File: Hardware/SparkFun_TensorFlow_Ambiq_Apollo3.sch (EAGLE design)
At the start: 102 parts, among them J5 CORTEX_DEBUG_PTH, J6 CAMERA-OV7670, M1 MEMS_MIC, M2 MEMS_MIC, U1 AMBIQ-APOLLO3KBR, U2 LIS2DH12, U3 1.8V, U4 LMV358, Y1 32MHz, Y2 32.768kHz

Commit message: Updating components to SparkFun ibraries
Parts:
- C1: device ambiq:0.47UF-0402-TIGHT-6.3V-10% -> SparkFun-Capacitors:470NF-0402_TIGHT-6.3V-10%-X5R
- C11: device ambiq:47NF-0402-TIGHT-25V-10% -> SparkFun-Capacitors:47NF-0402_TIGHT-25V-10%-X7R
- C16, C3, C5, C8: device ambiq:2.2UF-0402-TIGHT-25V-10% -> SparkFun-Capacitors:2.2UF-0402_TIGHT-10V-10%-X5R
- C18: device ambiq:0.5PF-0402-0.5PF-1% -> SparkFun-Capacitors:0.5PF-0402_TIGHT-20V-PM0.05PF-NP0
- C2: device ambiq:4.7UF-0402-TIGHT-6.3V-(20%) -> SparkFun-Capacitors:4.7UF-0402_TIGHT-6.3V-20%-X5R
- C28: device ambiq:1.0NF/1000PF-0402-50V-10% -> SparkFun-Capacitors:1.0NF/1000PF-0402_TIGHT-50V-10%
- J6: device ambiq:CAMERA-OV7670 -> SparkFun-Connectors:CAMERA-OV7670
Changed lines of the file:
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@@
 <part name="L2" library="ambiq" deviceset="INDUCTOR" device="-0805-1.0UH" value="1.0uH"/>
 <part name="GND3" library="SparkFun-PowerSymbols" deviceset="GND" device=""/>
-<part name="C2" library="ambiq" deviceset="4.7UF" device="-0402-TIGHT-6.3V-(20%)" value="4.7uF"/>
+<part name="C2" library="SparkFun-Capacitors" deviceset="4.7UF" device="-0402_TIGHT-6.3V-20%-X5R" value="4.7uF"/>
 <part name="C4" library="ambiq" deviceset="1.0UF" device="-0402-TIGHT-16V-10%" value="1.0uF"/>
 <part name="GND6" library="SparkFun-PowerSymbols" deviceset="GND" device=""/>
@@
 <part name="GND16" library="SparkFun-PowerSymbols" deviceset="GND" device=""/>
 <part name="R3" library="ambiq" deviceset="10KOHM" device="-0402-TIGHT-1/10W-1%" value="10k"/>
-<part name="C1" library="ambiq" deviceset="0.47UF" device="-0402-TIGHT-6.3V-10%" value="0.47uF"/>
-<part name="C3" library="ambiq" deviceset="2.2UF" device="-0402-TIGHT-25V-10%" value="2.2uF"/>
-<part name="C5" library="ambiq" deviceset="2.2UF" device="-0402-TIGHT-25V-10%" value="2.2uF"/>
-<part name="C8" library="ambiq" deviceset="2.2UF" device="-0402-TIGHT-25V-10%" value="2.2uF"/>
+<part name="C1" library="SparkFun-Capacitors" deviceset="470NF" device="-0402_TIGHT-6.3V-10%-X5R" value="0.47uF"/>
+<part name="C3" library="SparkFun-Capacitors" deviceset="2.2UF" device="-0402_TIGHT-10V-10%-X5R" value="2.2uF"/>
+<part name="C5" library="SparkFun-Capacitors" deviceset="2.2UF" device="-0402_TIGHT-10V-10%-X5R" value="2.2uF"/>
+<part name="C8" library="SparkFun-Capacitors" deviceset="2.2UF" device="-0402_TIGHT-10V-10%-X5R" value="2.2uF"/>
 <part name="GND8" library="SparkFun-PowerSymbols" deviceset="GND" device=""/>
 <part name="GND7" library="SparkFun-PowerSymbols" deviceset="GND" device=""/>
@@
 <part name="C14" library="ambiq" deviceset="1.0UF" device="-0402-TIGHT-16V-10%" value="1.0uF"/>
 <part name="C15" library="ambiq" deviceset="1.0UF" device="-0402-TIGHT-16V-10%" value="1.0uF"/>
-<part name="C11" library="ambiq" deviceset="47NF" device="-0402-TIGHT-25V-10%" value="47nF"/>
-<part name="C16" library="ambiq" deviceset="2.2UF" device="-0402-TIGHT-25V-10%" value="2.2uF"/>
+<part name="C11" library="SparkFun-Capacitors" deviceset="47NF" device="-0402_TIGHT-25V-10%-X7R" value="47nF"/>
+<part name="C16" library="SparkFun-Capacitors" deviceset="2.2UF" device="-0402_TIGHT-10V-10%-X5R" value="2.2uF"/>
 <part name="GND10" library="SparkFun-PowerSymbols" deviceset="GND" device=""/>
 <part name="GND11" library="SparkFun-PowerSymbols" deviceset="GND" device=""/>
@@
 <part name="C17" library="ambiq" deviceset="DNP-CAP" device="-0402-TIGHT" value="DNP"/>
 <part name="L3" library="ambiq" deviceset="INDUCTOR" device="-0402-2.7NH" value="2.7nH"/>
-<part name="C18" library="ambiq" deviceset="0.5PF" device="-0402-0.5PF-1%" value="0.5pF"/>
+<part name="C18" library="SparkFun-Capacitors" deviceset="0.5PF" device="-0402_TIGHT-20V-PM0.05PF-NP0" value="0.5pF"/>
 <part name="L4" library="ambiq" deviceset="INDUCTOR" device="-0402-2.0NH" value="2.0nH"/>
 <part name="GND21" library="SparkFun-PowerSymbols" deviceset="GND" device=""/>
@@
 <part name="M1" library="ambiq" deviceset="MEMS_MICROPHONE" device="SPW2430HR5H-B" value="MEMS_MIC"/>
 <part name="M2" library="ambiq" deviceset="MEMS_MICROPHONE" device="SPW2430HR5H-B" value="MEMS_MIC"/>
-<part name="J6" library="ambiq" deviceset="CAMERA-OV7670" device=""/>
+<part name="J6" library="SparkFun-Connectors" deviceset="CAMERA-OV7670" device=""/>
 <part name="BT1" library="SparkFun-Batteries" deviceset="BATTERY" device="-20MM_SMD_4LEGS_OVERPASTE_INNER"/>
 <part name="H4" library="SparkFun-Hardware" deviceset="STAND-OFF" device=""/>
@@
 <part name="TP1" library="SparkFun-Connectors" deviceset="TEST-POINT" device="3X5"/>
 <part name="TP2" library="SparkFun-Connectors" deviceset="TEST-POINT" device="3X5"/>
-<part name="C28" library="ambiq" deviceset="1.0NF/1000PF" device="-0402-50V-10%" value="1.0nF"/>
+<part name="C28" library="SparkFun-Capacitors" deviceset="1.0NF/1000PF" device="-0402_TIGHT-50V-10%" value="1.0nF"/>
 <part name="GND42" library="SparkFun-PowerSymbols" deviceset="GND" device=""/>
 <part name="TP3" library="SparkFun-Connectors" deviceset="TEST-POINT" device="3X5"/>

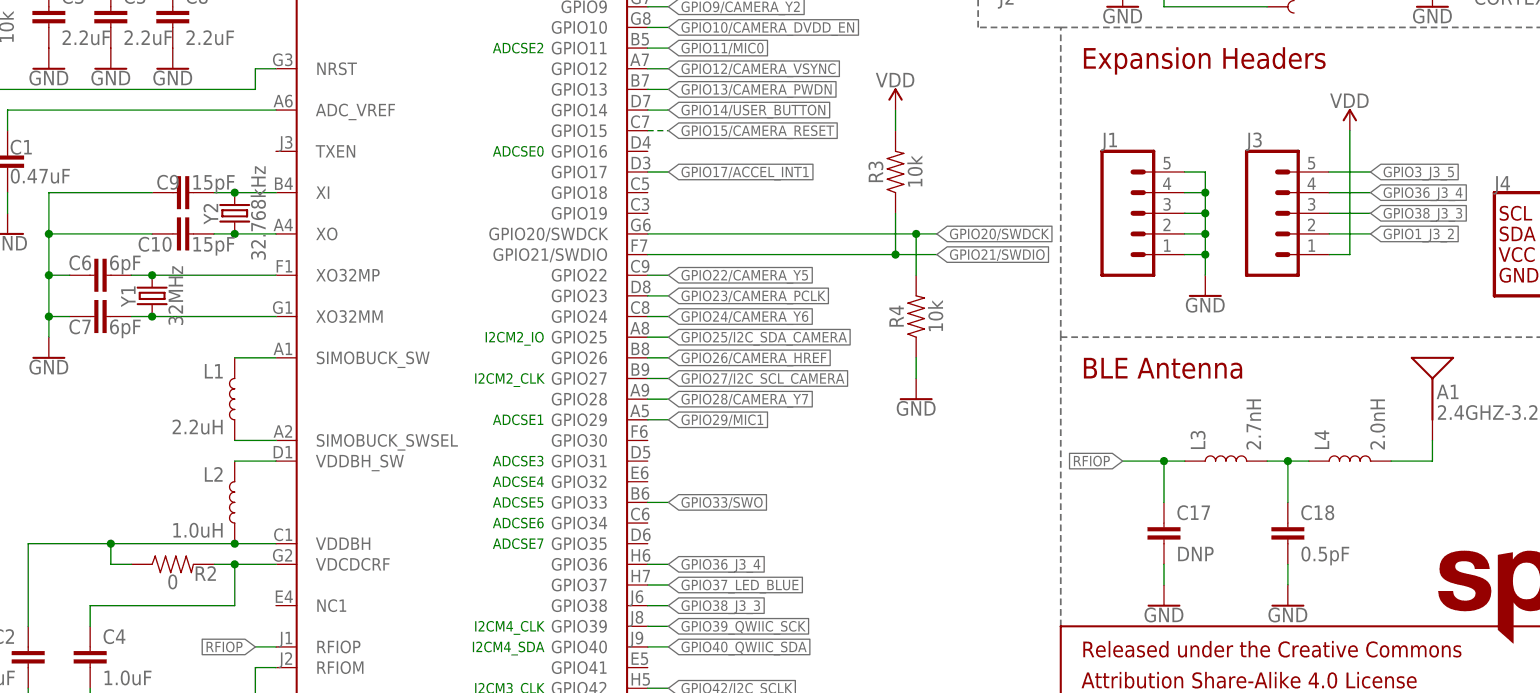
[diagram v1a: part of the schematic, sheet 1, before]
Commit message: Continue adding parts from SparkFun library
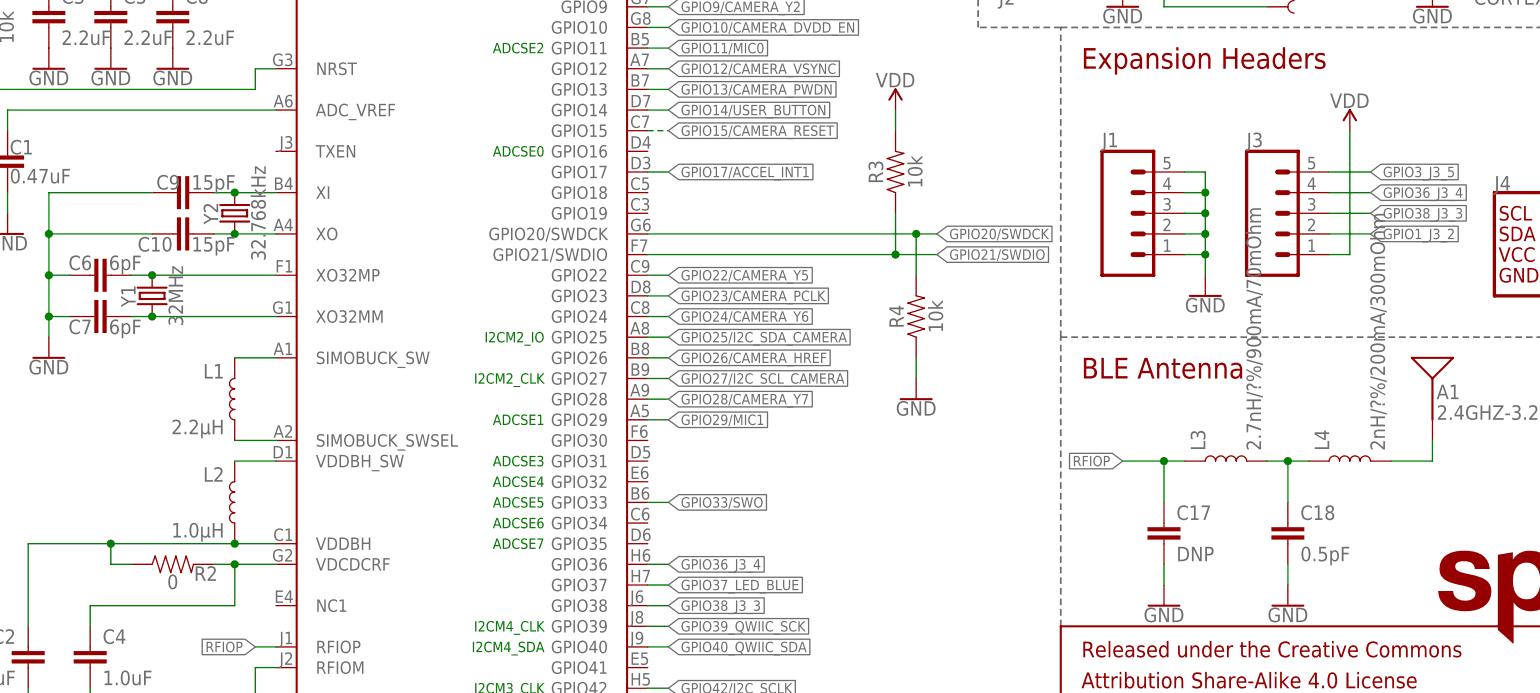
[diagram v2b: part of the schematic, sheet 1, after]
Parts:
- L1: value 2.2uH -> 2.2μH; device ambiq:INDUCTOR-0805-2.2UH -> SparkFun-Coils:2.2μH-0805_WIDE-2.2μH-1.7A-0.14OHM
- L2: value 1.0uH -> 1.0μH; device ambiq:INDUCTOR-0805-1.0UH -> SparkFun-Coils:1.0μH-0805_WIDE-1.0μH-1.4A-0.07OHM
- L3: value 2.7nH -> 2.7nH/?%/900mA/70mOhm; device ambiq:INDUCTOR-0402-2.7NH -> SparkFun-Coils:INDUCTOR-0402_TIGHT-2.7NH
- L4: value 2.0nH -> 2nH/?%/200mA/300mOhm; device ambiq:INDUCTOR-0402-2.0NH -> SparkFun-Coils:INDUCTOR-0402_TIGHT-2.0NH
- M1, M2: device ambiq:MEMS_MICROPHONESPW2430HR5H-B -> SparkFun-Sensors:MEMS_MICROPHONESPW2430HR5H-B
- R18: device ambiq:22KOHM-0402-1/16W-1% -> SparkFun-Resistors:22KOHM-0402_TIGHT-1/10W-1%
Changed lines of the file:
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@@
 <part name="R1" library="ambiq" deviceset="10KOHM" device="-0402-TIGHT-1/10W-1%" value="10k"/>
 <part name="GND5" library="SparkFun-PowerSymbols" deviceset="GND" device=""/>
-<part name="L1" library="ambiq" deviceset="INDUCTOR" device="-0805-2.2UH" value="2.2uH"/>
-<part name="L2" library="ambiq" deviceset="INDUCTOR" device="-0805-1.0UH" value="1.0uH"/>
+<part name="L1" library="SparkFun-Coils" deviceset="2.2μH" device="-0805_WIDE-2.2μH-1.7A-0.14OHM" value="2.2μH"/>
+<part name="L2" library="SparkFun-Coils" deviceset="1.0μH" device="-0805_WIDE-1.0μH-1.4A-0.07OHM" value="1.0μH"/>
 <part name="GND3" library="SparkFun-PowerSymbols" deviceset="GND" device=""/>
 <part name="C2" library="SparkFun-Capacitors" deviceset="4.7UF" device="-0402_TIGHT-6.3V-20%-X5R" value="4.7uF"/>
@@
 <part name="GND15" library="SparkFun-PowerSymbols" deviceset="GND" device=""/>
 <part name="C17" library="ambiq" deviceset="DNP-CAP" device="-0402-TIGHT" value="DNP"/>
-<part name="L3" library="ambiq" deviceset="INDUCTOR" device="-0402-2.7NH" value="2.7nH"/>
+<part name="L3" library="SparkFun-Coils" deviceset="INDUCTOR" device="-0402_TIGHT-2.7NH" value="2.7nH/?%/900mA/70mOhm"/>
 <part name="C18" library="SparkFun-Capacitors" deviceset="0.5PF" device="-0402_TIGHT-20V-PM0.05PF-NP0" value="0.5pF"/>
-<part name="L4" library="ambiq" deviceset="INDUCTOR" device="-0402-2.0NH" value="2.0nH"/>
+<part name="L4" library="SparkFun-Coils" deviceset="INDUCTOR" device="-0402_TIGHT-2.0NH" value="2nH/?%/200mA/300mOhm"/>
 <part name="GND21" library="SparkFun-PowerSymbols" deviceset="GND" device=""/>
 <part name="GND17" library="SparkFun-PowerSymbols" deviceset="GND" device=""/>
@@
 <part name="GND24" library="SparkFun-PowerSymbols" deviceset="GND" device=""/>
 <part name="R2" library="ambiq" deviceset="0OHM" device="-0402-TIGHT-1/10W-5%" value="0"/>
-<part name="M1" library="ambiq" deviceset="MEMS_MICROPHONE" device="SPW2430HR5H-B" value="MEMS_MIC"/>
-<part name="M2" library="ambiq" deviceset="MEMS_MICROPHONE" device="SPW2430HR5H-B" value="MEMS_MIC"/>
+<part name="M1" library="SparkFun-Sensors" deviceset="MEMS_MICROPHONE" device="SPW2430HR5H-B" value="MEMS_MIC"/>
+<part name="M2" library="SparkFun-Sensors" deviceset="MEMS_MICROPHONE" device="SPW2430HR5H-B" value="MEMS_MIC"/>
 <part name="J6" library="SparkFun-Connectors" deviceset="CAMERA-OV7670" device=""/>
 <part name="BT1" library="SparkFun-Batteries" deviceset="BATTERY" device="-20MM_SMD_4LEGS_OVERPASTE_INNER"/>
@@
 <part name="GND25" library="SparkFun-PowerSymbols" deviceset="GND" device=""/>
 <part name="R19" library="ambiq" deviceset="10KOHM" device="-0402-TIGHT-1/10W-1%" value="10k"/>
-<part name="R18" library="ambiq" deviceset="22KOHM" device="-0402-1/16W-1%" value="22k"/>
+<part name="R18" library="SparkFun-Resistors" deviceset="22KOHM" device="-0402_TIGHT-1/10W-1%" value="22k"/>
 <part name="SUPPLY31" library="SparkFun-PowerSymbols" deviceset="VDD" device=""/>
 <part name="GND37" library="SparkFun-PowerSymbols" deviceset="GND" device=""/>

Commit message: Finish converting parts to SparkFun library
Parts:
- R1, R10, R11, R19, R22, R25, R26, R3, R4, R9: device ambiq:10KOHM-0402-TIGHT-1/10W-1% -> SparkFun-Resistors:10KOHM-0402_TIGHT-1/10W-1%
- R2: device ambiq:0OHM-0402-TIGHT-1/10W-5% -> SparkFun-Resistors:0OHM-0402_TIGHT-1/16W
- U1: device ambiq:AMBIQ-APOLLO3KBR -> SparkFun-IC-Microcontroller:AMBIQ-APOLLO3KBR
- U2: device ambiq:LIS2DH12 -> SparkFun-Sensors:LIS2DH12
- U3: device ambiq:V_REG_AP2127K-2.8 -> SparkFun-IC-Power:V_REG_AP2127K-1.8V
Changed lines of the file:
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@@
 </classes>
 <parts>
-<part name="U1" library="ambiq" deviceset="AMBIQ-APOLLO3" device="KBR"/>
+<part name="U1" library="SparkFun-IC-Microcontroller" deviceset="AMBIQ-APOLLO3" device="KBR"/>
 <part name="FRAME1" library="SparkFun-Aesthetics" deviceset="FRAME-LETTER" device=""/>
 <part name="J2" library="SparkFun-Connectors" deviceset="6_PIN_SERIAL_TARGET" device="SMD"/>
@@
 <part name="C9" library="ambiq" deviceset="15PF" device="-0402-TIGHT-50V-5%" value="15pF"/>
 <part name="C10" library="ambiq" deviceset="15PF" device="-0402-TIGHT-50V-5%" value="15pF"/>
-<part name="R1" library="ambiq" deviceset="10KOHM" device="-0402-TIGHT-1/10W-1%" value="10k"/>
+<part name="R1" library="SparkFun-Resistors" deviceset="10KOHM" device="-0402_TIGHT-1/10W-1%" value="10k"/>
 <part name="GND5" library="SparkFun-PowerSymbols" deviceset="GND" device=""/>
 <part name="L1" library="SparkFun-Coils" deviceset="2.2μH" device="-0805_WIDE-2.2μH-1.7A-0.14OHM" value="2.2μH"/>
@@
 <part name="GND9" library="SparkFun-PowerSymbols" deviceset="GND" device=""/>
 <part name="GND2" library="SparkFun-PowerSymbols" deviceset="GND" device=""/>
-<part name="R4" library="ambiq" deviceset="10KOHM" device="-0402-TIGHT-1/10W-1%" value="10k"/>
+<part name="R4" library="SparkFun-Resistors" deviceset="10KOHM" device="-0402_TIGHT-1/10W-1%" value="10k"/>
 <part name="GND16" library="SparkFun-PowerSymbols" deviceset="GND" device=""/>
-<part name="R3" library="ambiq" deviceset="10KOHM" device="-0402-TIGHT-1/10W-1%" value="10k"/>
+<part name="R3" library="SparkFun-Resistors" deviceset="10KOHM" device="-0402_TIGHT-1/10W-1%" value="10k"/>
 <part name="C1" library="SparkFun-Capacitors" deviceset="470NF" device="-0402_TIGHT-6.3V-10%-X5R" value="0.47uF"/>
 <part name="C3" library="SparkFun-Capacitors" deviceset="2.2UF" device="-0402_TIGHT-10V-10%-X5R" value="2.2uF"/>
@@
 <part name="J5" library="SparkFun-Connectors" deviceset="CORTEX_DEBUG" device="_PTH" value="CORTEX_DEBUG_PTH"/>
 <part name="GND24" library="SparkFun-PowerSymbols" deviceset="GND" device=""/>
-<part name="R2" library="ambiq" deviceset="0OHM" device="-0402-TIGHT-1/10W-5%" value="0"/>
+<part name="R2" library="SparkFun-Resistors" deviceset="0OHM" device="-0402_TIGHT-1/16W" value="0"/>
 <part name="M1" library="SparkFun-Sensors" deviceset="MEMS_MICROPHONE" device="SPW2430HR5H-B" value="MEMS_MIC"/>
 <part name="M2" library="SparkFun-Sensors" deviceset="MEMS_MICROPHONE" device="SPW2430HR5H-B" value="MEMS_MIC"/>
@@
 <part name="SUPPLY1" library="SparkFun-PowerSymbols" deviceset="V_BATT" device=""/>
 <part name="GND1" library="SparkFun-PowerSymbols" deviceset="GND" device=""/>
-<part name="U2" library="ambiq" deviceset="LIS2DH12" device=""/>
+<part name="U2" library="SparkFun-Sensors" deviceset="LIS2DH12" device=""/>
 <part name="C21" library="SparkFun-Capacitors" deviceset="10UF" device="-0603-6.3V-20%" value="10uF"/>
 <part name="C20" library="ambiq" deviceset="0.1UF" device="-0402-TIGHT-16V-10%" value="0.1uF"/>
@@
 <part name="SUPPLY22" library="SparkFun-PowerSymbols" deviceset="VDD" device=""/>
 <part name="GND32" library="SparkFun-PowerSymbols" deviceset="GND" device=""/>
-<part name="R10" library="ambiq" deviceset="10KOHM" device="-0402-TIGHT-1/10W-1%" value="10k"/>
+<part name="R10" library="SparkFun-Resistors" deviceset="10KOHM" device="-0402_TIGHT-1/10W-1%" value="10k"/>
 <part name="SUPPLY18" library="SparkFun-PowerSymbols" deviceset="VDD" device=""/>
 <part name="SUPPLY21" library="SparkFun-PowerSymbols" deviceset="VDD" device=""/>
@@
 <part name="SUPPLY4" library="SparkFun-PowerSymbols" deviceset="VDD" device=""/>
 <part name="SUPPLY20" library="SparkFun-PowerSymbols" deviceset="1.8V" device=""/>
-<part name="U3" library="ambiq" deviceset="V_REG_AP2127" device="K-2.8" value="1.8V"/>
+<part name="U3" library="SparkFun-IC-Power" deviceset="V_REG_AP2127" device="K-1.8V" value="1.8V"/>
 <part name="SUPPLY24" library="SparkFun-PowerSymbols" deviceset="VDD" device=""/>
 <part name="GND34" library="SparkFun-PowerSymbols" deviceset="GND" device=""/>
@@
 <part name="GND27" library="SparkFun-PowerSymbols" deviceset="GND" device=""/>
 <part name="GND26" library="SparkFun-PowerSymbols" deviceset="GND" device=""/>
-<part name="R9" library="ambiq" deviceset="10KOHM" device="-0402-TIGHT-1/10W-1%" value="10k"/>
+<part name="R9" library="SparkFun-Resistors" deviceset="10KOHM" device="-0402_TIGHT-1/10W-1%" value="10k"/>
 <part name="SUPPLY15" library="SparkFun-PowerSymbols" deviceset="VDD" device=""/>
 <part name="D4" library="SparkFun-LED" deviceset="LED-BLUE" device="0603" value="BLUE"/>
@@
 <part name="GND23" library="SparkFun-PowerSymbols" deviceset="GND" device=""/>
 <part name="GND25" library="SparkFun-PowerSymbols" deviceset="GND" device=""/>
-<part name="R19" library="ambiq" deviceset="10KOHM" device="-0402-TIGHT-1/10W-1%" value="10k"/>
+<part name="R19" library="SparkFun-Resistors" deviceset="10KOHM" device="-0402_TIGHT-1/10W-1%" value="10k"/>
 <part name="R18" library="SparkFun-Resistors" deviceset="22KOHM" device="-0402_TIGHT-1/10W-1%" value="22k"/>
 <part name="SUPPLY31" library="SparkFun-PowerSymbols" deviceset="VDD" device=""/>
@@
 <part name="GND18" library="SparkFun-PowerSymbols" deviceset="GND" device=""/>
 <part name="SUPPLY13" library="SparkFun-PowerSymbols" deviceset="VDD" device=""/>
-<part name="R11" library="ambiq" deviceset="10KOHM" device="-0402-TIGHT-1/10W-1%" value="10k"/>
+<part name="R11" library="SparkFun-Resistors" deviceset="10KOHM" device="-0402_TIGHT-1/10W-1%" value="10k"/>
 <part name="GND33" library="SparkFun-PowerSymbols" deviceset="GND" device=""/>
 <part name="FRAME2" library="SparkFun-Aesthetics" deviceset="FRAME-LETTER" device="NO_PACKAGE">
@@
 <part name="LOGO1" library="SparkFun-Aesthetics" deviceset="SFE_LOGO_NAME_FLAME" device=".1_INCH"/>
 <part name="LOGO2" library="SparkFun-Aesthetics" deviceset="OSHW-LOGO" device="S"/>
-<part name="R22" library="ambiq" deviceset="10KOHM" device="-0402-TIGHT-1/10W-1%" value="10k"/>
+<part name="R22" library="SparkFun-Resistors" deviceset="10KOHM" device="-0402_TIGHT-1/10W-1%" value="10k"/>
 <part name="GND40" library="SparkFun-PowerSymbols" deviceset="GND" device=""/>
 <part name="J4" library="SparkFun-Connectors" deviceset="QWIIC_CONNECTOR" device="JS-1MM"/>
@@
 <part name="SUPPLY36" library="SparkFun-PowerSymbols" deviceset="VDD" device=""/>
 <part name="SUPPLY37" library="SparkFun-PowerSymbols" deviceset="VDD" device=""/>
-<part name="R25" library="ambiq" deviceset="10KOHM" device="-0402-TIGHT-1/10W-1%" value="10k"/>
-<part name="R26" library="ambiq" deviceset="10KOHM" device="-0402-TIGHT-1/10W-1%" value="10k"/>
+<part name="R25" library="SparkFun-Resistors" deviceset="10KOHM" device="-0402_TIGHT-1/10W-1%" value="10k"/>
+<part name="R26" library="SparkFun-Resistors" deviceset="10KOHM" device="-0402_TIGHT-1/10W-1%" value="10k"/>
 <part name="SUPPLY38" library="SparkFun-PowerSymbols" deviceset="VDD" device=""/>
 <part name="SUPPLY39" library="SparkFun-PowerSymbols" deviceset="VDD" device=""/>
